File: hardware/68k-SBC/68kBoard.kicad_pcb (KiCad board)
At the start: 2 copper layers, 154.9 x 139.7 mm, 78 parts, among them J1 ADBUS, J2 Barrel_Jack, J3 SIGBUS, J4 Serial1, J5 Serial2, SW1 RESET, SW2 IP2, SW3 IP3, U1 L7805, U10 HM628512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

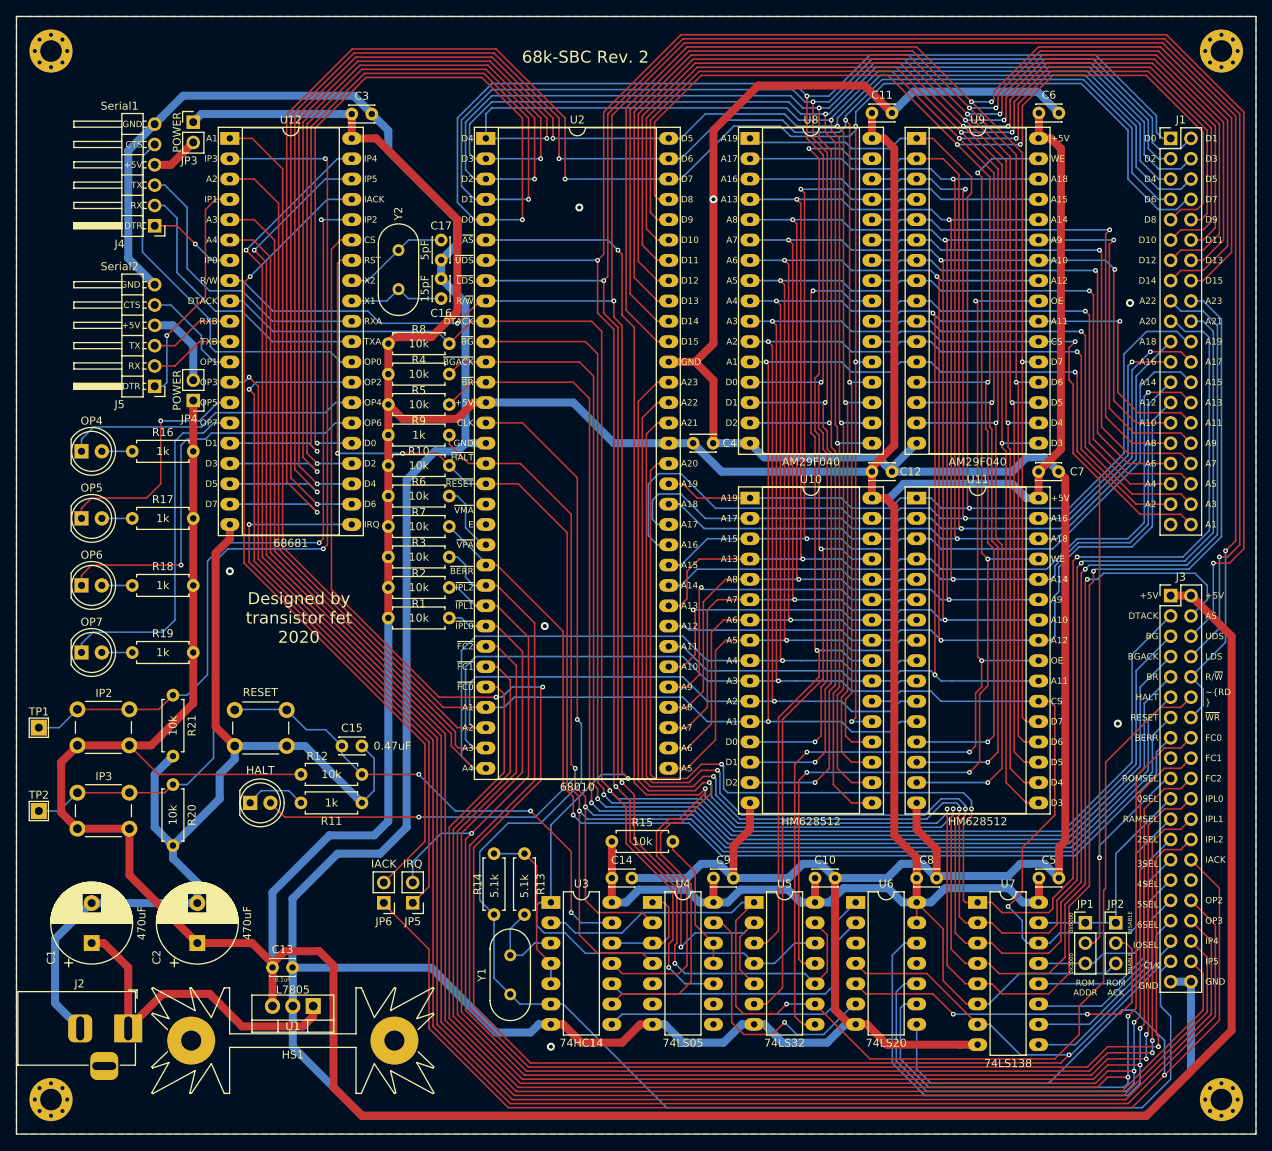
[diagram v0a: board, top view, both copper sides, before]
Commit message: Upgraded project formats to kicad 6.0
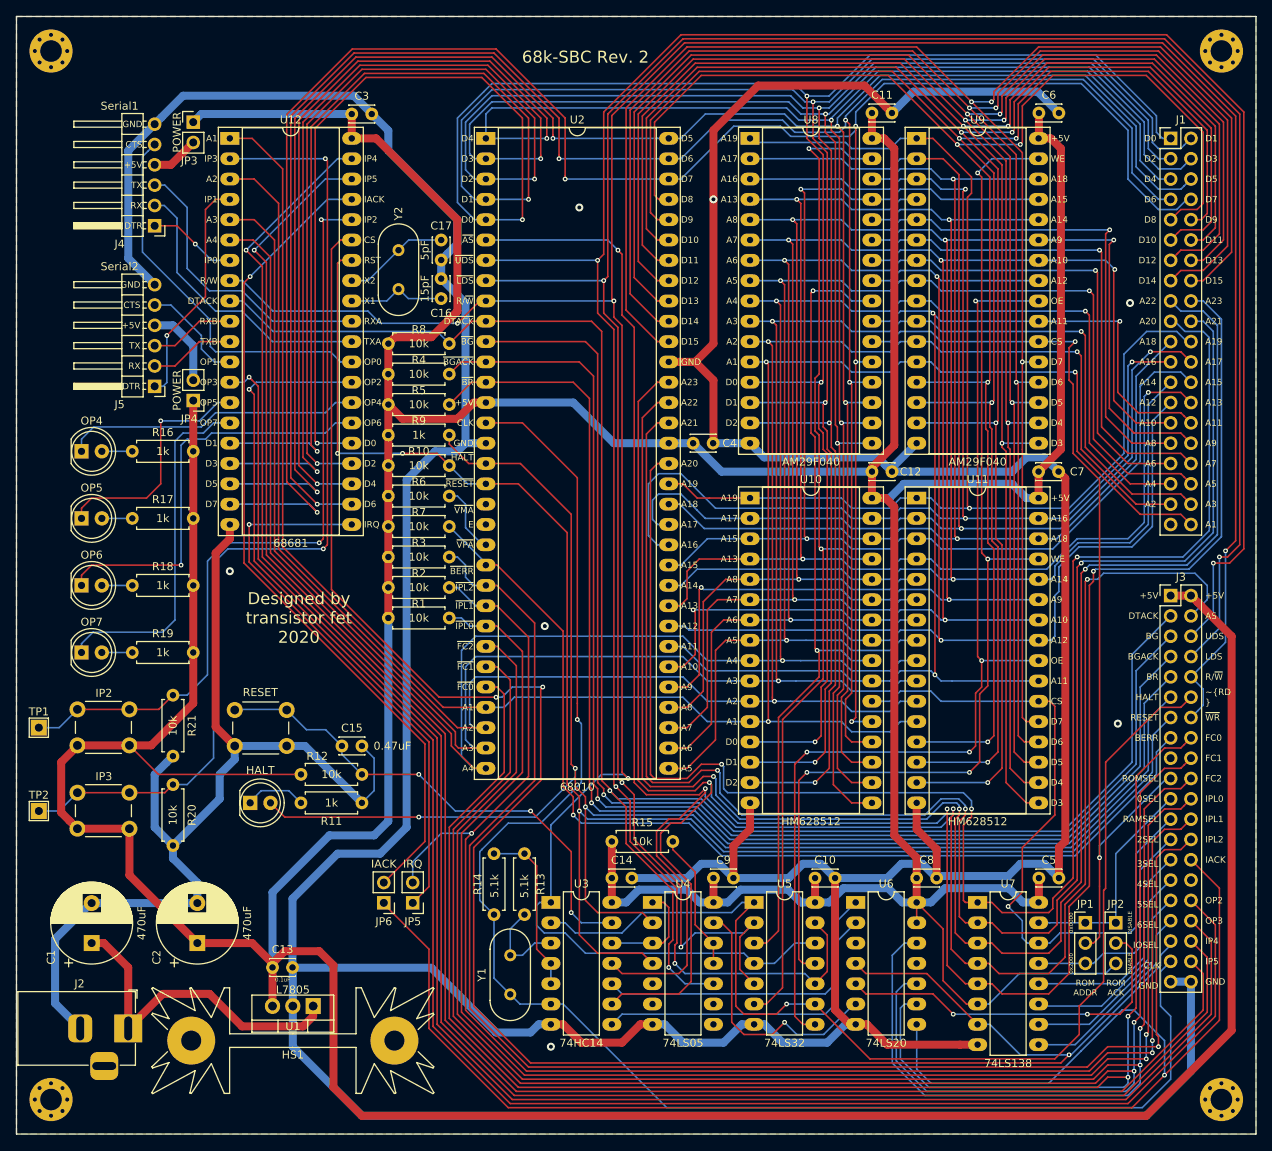
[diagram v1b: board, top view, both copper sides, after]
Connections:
- net R~W renamed R~{W}
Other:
- net class Default removed
- board text added: "R/~{W}"
- board text added: "~{AS}"
- board text added: "~{BERR}"
- board text added: "~{BGACK}"
- board text added: "~{BG}"
- board text added: "~{BR}"
- board text added: "~{DTACK}"
- board text added: "~{FC0}"
- board text added: "~{FC1}"
- board text added: "~{FC2}"
- board text added: "~{HALT}"
- board text added: "~{IPL0}"
- board text added: "~{IPL1}"
- board text added: "~{IPL2}"
- board text added: "~{LDS}"
- board text added: "~{RD }"
- board text added: "~{RESET}"
- board text added: "~{UDS}"
- board text added: "~{VMA}"
- board text added: "~{VPA}"
- board text added: "~{WR}"
- board text removed: "R/~W"
- board text removed: "~AS"
- board text removed: "~BERR"
- board text removed: "~BG"
- board text removed: "~BGACK"
- board text removed: "~BR"
- board text removed: "~DTACK"
- board text removed: "~FC0"
- board text removed: "~FC1"
- board text removed: "~FC2"
- board text removed: "~HALT"
- board text removed: "~IPL0"
- board text removed: "~IPL1"
- board text removed: "~IPL2"
- board text removed: "~LDS"
- board text removed: "~RD"
- board text removed: "~RESET"
- board text removed: "~UDS"
- board text removed: "~VMA"
- board text removed: "~VPA"
- board text removed: "~WR"
